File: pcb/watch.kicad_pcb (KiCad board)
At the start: 2 copper layers, 2 parts, among them U1 nRF52840, U3 MAX-M10S

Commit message: sus2
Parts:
- added AE1: Antenna, JLCImport:KH-GPS181804-WY, F.Cu at (152.5, 97.0)
- added BT2: Battery_Cell, Connector_JST:JST_PH_S2B-PH-SM4-TB_1x02-1MP_P2.00mm_Horizontal, F.Cu at (172.7, 113.3)
- added C10: 12pF, Capacitor_SMD:C_0402_1005Metric, F.Cu at (167.6, 99.3)
- added C11: 12pF, Capacitor_SMD:C_0402_1005Metric, F.Cu at (167.6, 101.3)
- added C12: 1uF, Capacitor_SMD:C_0402_1005Metric, F.Cu at (170.5, 89.5)
- added C13: 47nF, Capacitor_SMD:C_0603_1608Metric, F.Cu at (164.2, 97.3)
- added C14: 100pF, Capacitor_SMD:C_0402_1005Metric, F.Cu at (170.5, 91.4)
- added C15: 4.7uF, Capacitor_SMD:C_0603_1608Metric, F.Cu at (164.2, 99.8)
- added C17: 12pF, Capacitor_SMD:C_0402_1005Metric, F.Cu at (170.5, 93.4)
- added C18: 12pF, Capacitor_SMD:C_0402_1005Metric, F.Cu at (170.5, 95.4)
- added C19: 10uF, Capacitor_SMD:C_0603_1608Metric, F.Cu at (164.2, 102.3)
- added C2: 100nF, Capacitor_SMD:C_0402_1005Metric, F.Cu at (167.6, 89.5)
- added C20: 22uF, Capacitor_SMD:C_0805_2012Metric, F.Cu at (151.2, 126.2)
- added C21: 1uF, Capacitor_SMD:C_0402_1005Metric, F.Cu at (170.5, 97.3)
- added C22: 1uF, Capacitor_SMD:C_0402_1005Metric, F.Cu at (170.5, 99.3)
- added C23: 1uF, Capacitor_SMD:C_0402_1005Metric, F.Cu at (170.5, 101.3)
- added C24: 4.7uF, Capacitor_SMD:C_0603_1608Metric, F.Cu at (164.2, 104.8)
- added C25: 100nF, Capacitor_SMD:C_0402_1005Metric, F.Cu at (173.3, 89.5)
- added C26: 1uF, Capacitor_SMD:C_0402_1005Metric, F.Cu at (173.3, 91.4)
- added C27: 100nF, Capacitor_SMD:C_0402_1005Metric, F.Cu at (173.3, 93.4)
- added C28: 100nF, Capacitor_SMD:C_0402_1005Metric, F.Cu at (173.3, 95.4)
- added C3: 100nF, Capacitor_SMD:C_0402_1005Metric, F.Cu at (167.6, 91.4)
- added C4: 100nF, Capacitor_SMD:C_0402_1005Metric, F.Cu at (167.6, 93.4)
- added C5: 100nF, Capacitor_SMD:C_0402_1005Metric, F.Cu at (167.6, 95.4)
- added C6: 100nF, Capacitor_SMD:C_0402_1005Metric, F.Cu at (167.6, 97.3)
- added C7: 4.7uF, Capacitor_SMD:C_0603_1608Metric, F.Cu at (164.2, 89.7)
- added C8: 4.7uF, Capacitor_SMD:C_0603_1608Metric, F.Cu at (164.2, 92.2)
- added C9: 4.7uF, Capacitor_SMD:C_0603_1608Metric, F.Cu at (164.2, 94.8)
- added D2: red, LED_SMD:LED_0603_1608Metric, F.Cu at (169.6, 126.2)
- added D3: green, LED_SMD:LED_0805_2012Metric, F.Cu at (145.2, 124.2)
- added F2: 1A/1.8A, Fuse:Fuse_1206_3216Metric_Pad1.42x1.75mm_HandSolder, F.Cu at (146.0, 121.0)
- added J1: USB_C_Receptacle_USB2.0_14P, Connector_USB:USB_C_Receptacle_G-Switch_GT-USB-7010ASV, F.Cu at (161.7, 113.0)
- added R3: 100k, Resistor_SMD:R_0402_1005Metric, F.Cu at (169.0, 119.9)
- added R6: 1.5k, Resistor_SMD:R_0402_1005Metric, F.Cu at (169.0, 121.9)
- added R7: 1.5k, Resistor_SMD:R_0402_1005Metric, F.Cu at (169.0, 123.9)
- added R8: 1.5k, Resistor_SMD:R_0402_1005Metric, F.Cu at (171.9, 119.9)
- added R9: 1.5k, Resistor_SMD:R_0402_1005Metric, F.Cu at (171.9, 121.9)
- added SW1: 10k, Resistor_SMD:R_0402_1005Metric, F.Cu at (171.9, 123.9)
- added SW2: 10k, Resistor_SMD:R_0402_1005Metric, F.Cu at (174.8, 119.9)
- added SW3: 10k, Resistor_SMD:R_0402_1005Metric, F.Cu at (174.8, 121.9)
- added SW4: 10k, Resistor_SMD:R_0402_1005Metric, F.Cu at (174.8, 123.9)
- added U4: nRF52840, Package_DFN_QFN:Nordic_AQFN-73-1EP_7x7mm_P0.5mm, F.Cu at (160.9, 122.8)
- added U5: MAX-M10S, RF_GPS:ublox_MAX, F.Cu at (149.4, 113.5)
- added U7: BQ24074RGT, Package_DFN_QFN:VQFN-16-1EP_3x3mm_P0.5mm_EP1.6x1.6mm, F.Cu at (152.0, 122.0)
- added U8: TPS7A20xxxDQN, Package_SON:Texas_X2SON-4_1x1mm_P0.65mm, F.Cu at (173.2, 126.2)
- added Y1: RV-3028-C7, Package_SON:MicroCrystal_C7_SON-8_1.5x3.2mm_P0.9mm, F.Cu at (168.3, 104.9)
- added Y2: USBLC6-2SC6, Package_TO_SOT_SMD:SOT-23-6, F.Cu at (172.8, 104.7)
- U1: value nRF52840 -> 5.1k; footprint Package_DFN_QFN:Nordic_AQFN-73-1EP_7x7mm_P0.5mm -> Resistor_SMD:R_0603_1608Metric_Pad0.98x0.95mm_HandSolder
- U3: value MAX-M10S -> SW_Push
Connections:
- U3 pad 11: unconnected-(U3-RF_IN-Pad11) -> Net-(AE1-A)
- U3 pad 18: unconnected-(U3-~{SAFEBOOT}-Pad18) -> P0.15
- U3 pad 2: unconnected-(U3-TXD-Pad2) -> P0.13
- U3 pad 3: unconnected-(U3-RXD-Pad3) -> P0.14
- U3 pad 6: unconnected-(U3-V_BCKP-Pad6) -> +3V3
- U3 pad 7: +3V3 -> +3V0_GPS
- U3 pad 8: +3V3 -> +3V0_GPS
- U3 pad 9: unconnected-(U3-~{RESET}-Pad9) -> P0.16

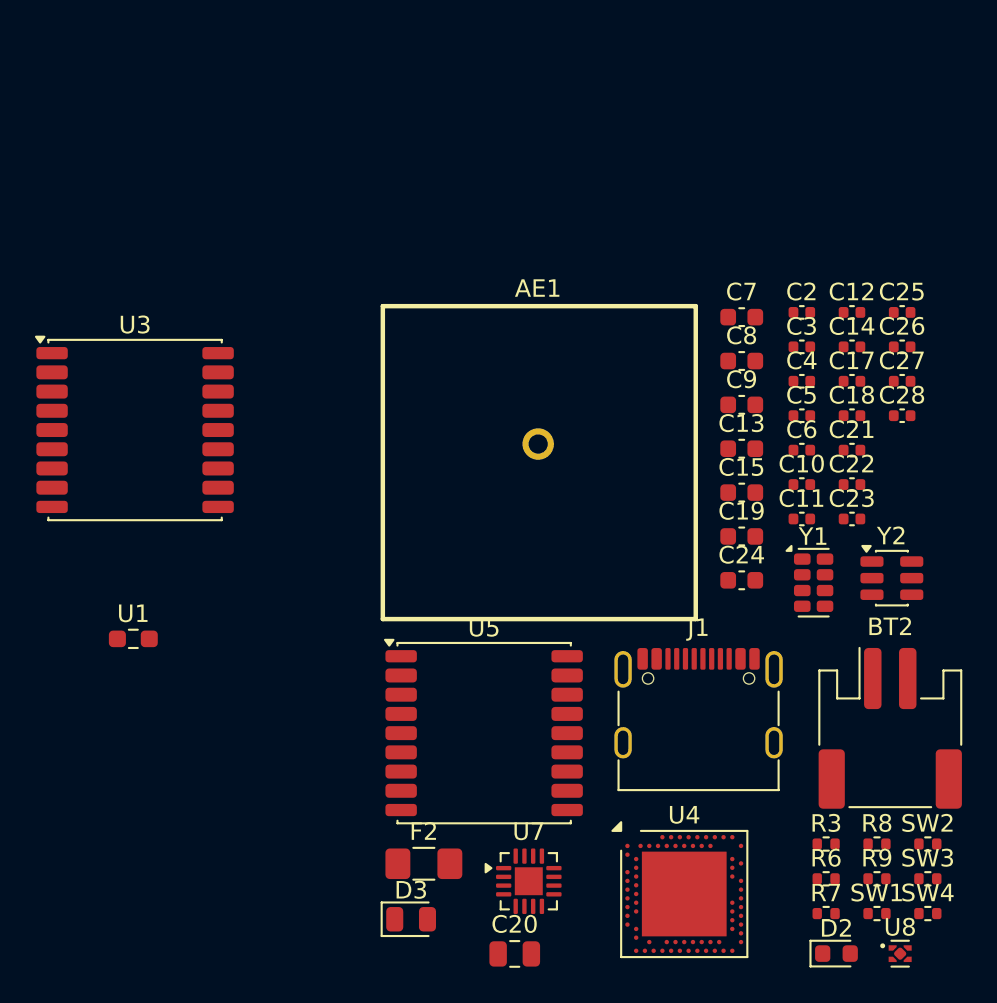
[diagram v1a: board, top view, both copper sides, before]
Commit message: fix symbols getting absolutely goofed up
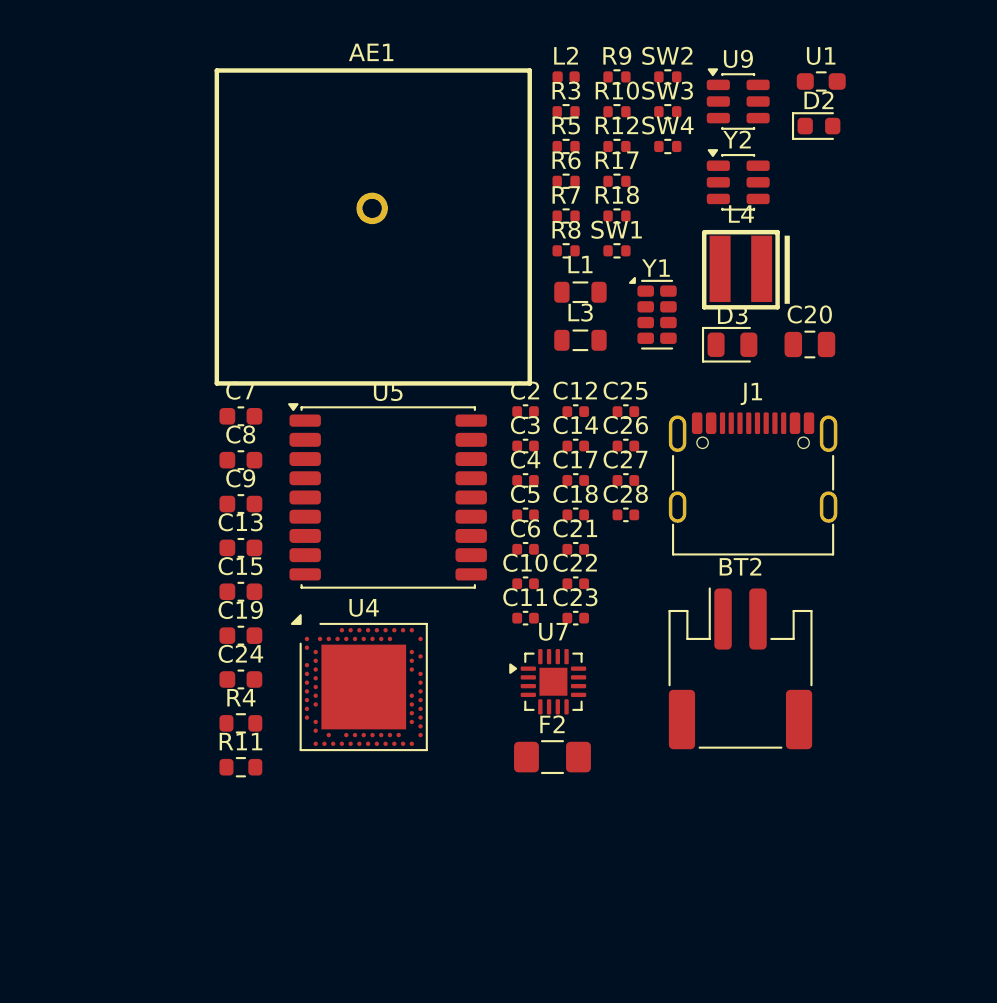
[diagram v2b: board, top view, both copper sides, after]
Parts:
- removed U3: SW_Push, RF_GPS:ublox_MAX
- removed U8: TPS7A20xxxDQN, Package_SON:Texas_X2SON-4_1x1mm_P0.65mm
- added L1: 10uH, Inductor_SMD:L_0805_2012Metric, F.Cu at (154.9, 88.3)
- added L2: 15nH, Inductor_SMD:L_0402_1005Metric, F.Cu at (154.1, 76.0)
- added L3: 10uH, Inductor_SMD:L_0805_2012Metric, F.Cu at (154.9, 91.1)
- added L4: 0.47uH, JLCImport:XFL4015-471MEC, F.Cu at (164.1, 87.0)
- added R10: 1.18k, Resistor_SMD:R_0402_1005Metric, F.Cu at (157.0, 78.0)
- added R11: 1.13k, Resistor_SMD:R_0603_1608Metric, F.Cu at (135.5, 115.5)
- added R12: 46.4k, Resistor_SMD:R_0402_1005Metric, F.Cu at (157.0, 80.0)
- added R17: 4.12k, Resistor_SMD:R_0402_1005Metric, F.Cu at (157.0, 82.0)
- added R18: 4.12k, Resistor_SMD:R_0402_1005Metric, F.Cu at (157.0, 84.0)
- added R4: 511k, Resistor_SMD:R_0603_1608Metric, F.Cu at (135.5, 113.0)
- added R5: 91k, Resistor_SMD:R_0402_1005Metric, F.Cu at (154.1, 80.0)
- added U9: USBLC6-2SC6, Package_TO_SOT_SMD:SOT-23-6, F.Cu at (164.0, 77.4)
- Y2: value USBLC6-2SC6 -> 32.768KHz
- moved U1 50.7 mm to (168.7, 76.3)
- moved R9 48.2 mm to (157.0, 76.0)
- moved D2 47.4 mm to (168.6, 78.8)
- moved SW4 46.3 mm to (159.9, 80.0)
- moved SW2 46.3 mm to (159.9, 76.0)
- moved SW3 46.3 mm to (159.9, 78.0)
- moved R3 44.5 mm to (154.1, 78.0)
- moved R7 42.6 mm to (154.1, 84.0)
- moved R6 42.6 mm to (154.1, 82.0)
- moved SW1 40.7 mm to (157.0, 85.9)
- moved C20 38.7 mm to (168.1, 91.3)
- moved R8 38.3 mm to (154.1, 85.9)
- moved D3 37.7 mm to (163.6, 91.3)
- moved C13 29.2 mm to (135.5, 102.9)
- moved C15 29.2 mm to (135.5, 105.5)
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
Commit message: sussy
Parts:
- removed AE1: Antenna, JLCImport:KH-GPS181804-WY
- removed BT2: Battery_Cell, Connector_JST:JST_PH_S2B-PH-SM4-TB_1x02-1MP_P2.00mm_Horizontal
- removed C23: 1uF, Capacitor_SMD:C_0402_1005Metric
- removed C24: 4.7uF, Capacitor_SMD:C_0603_1608Metric
- removed D3: green, LED_SMD:LED_0805_2012Metric
- removed F2: 1A/1.8A, Fuse:Fuse_1206_3216Metric_Pad1.42x1.75mm_HandSolder
- removed R17, R18: 4.12k, Resistor_SMD:R_0402_1005Metric
- removed U7: BQ24074RGT, Package_DFN_QFN:VQFN-16-1EP_3x3mm_P0.5mm_EP1.6x1.6mm
- removed U9: USBLC6-2SC6, Package_TO_SOT_SMD:SOT-23-6
- removed the Y1 at (159.3, 89.6)
- removed the Y2 at (164.0, 82.0)
- added BT1: Battery_Cell, Connector_JST:JST_PH_S2B-PH-SM4-TB_1x02-1MP_P2.00mm_Horizontal, F.Cu at (162.7, 95.6)
- added C1: 100nF, Capacitor_SMD:C_0402_1005Metric, F.Cu at (150.4, 81.0)
- added C16: 22pF, Capacitor_SMD:C_0402_1005Metric, F.Cu at (153.3, 82.9)
- added D1: green, LED_SMD:LED_0805_2012Metric, F.Cu at (151.3, 107.1)
- added F1: 1A/1.8A, Fuse:Fuse_1206_3216Metric_Pad1.42x1.75mm_HandSolder, F.Cu at (152.0, 103.9)
- added R1: 4.12k, Resistor_SMD:R_0402_1005Metric, F.Cu at (162.0, 85.0)
- added R2: 4.12k, Resistor_SMD:R_0402_1005Metric, F.Cu at (162.0, 87.0)
- added U2: USBLC6-2SC6, Package_TO_SOT_SMD:SOT-23-6, F.Cu at (160.2, 103.6)
- added U3: MAX-M10S, RF_GPS:ublox_MAX, F.Cu at (172.8, 83.9)
- added U6: BQ24074RGT, Package_DFN_QFN:VQFN-16-1EP_3x3mm_P0.5mm_EP1.6x1.6mm, F.Cu at (152.0, 94.4)
- added U8: RV-3028-C7, Package_SON:MicroCrystal_C7_SON-8_1.5x3.2mm_P0.9mm, F.Cu at (151.1, 99.8)
- added Y1: RV-3028-C7, Package_SON:MicroCrystal_C7_SON-8_1.5x3.2mm_P0.9mm, F.Cu at (155.1, 99.8)
- added Y1: 32MHz, Crystal:Crystal_SMD_2016-4Pin_2.0x1.6mm, F.Cu at (169.0, 75.3)
- added Y2: 32.768KHz, Package_TO_SOT_SMD:SOT-23-6, F.Cu at (160.2, 108.2)
- added Y2: 32.768KHz, JLCImport:Q13FC1350000400, F.Cu at (152.2, 110.9)
- C10, C11: value 12pF -> 4.7uF; footprint Capacitor_SMD:C_0402_1005Metric -> Capacitor_SMD:C_0603_1608Metric
- C12, C22: value 1uF -> 4.7uF; footprint Capacitor_SMD:C_0402_1005Metric -> Capacitor_SMD:C_0603_1608Metric
- C13: value 47nF -> 1uF; footprint Capacitor_SMD:C_0603_1608Metric -> Capacitor_SMD:C_0402_1005Metric
- C14: value 100pF -> 47nF; footprint Capacitor_SMD:C_0402_1005Metric -> Capacitor_SMD:C_0603_1608Metric
- C15: value 4.7uF -> 22pF; footprint Capacitor_SMD:C_0603_1608Metric -> Capacitor_SMD:C_0402_1005Metric
- C17: value 12pF -> 10uF; footprint Capacitor_SMD:C_0402_1005Metric -> Capacitor_SMD:C_0603_1608Metric
- C18: value 12pF -> 1uF
- C19: value 10uF -> 1uF; footprint Capacitor_SMD:C_0603_1608Metric -> Capacitor_SMD:C_0402_1005Metric
- C2: value 100nF -> 4.7uF; footprint Capacitor_SMD:C_0402_1005Metric -> Capacitor_SMD:C_0603_1608Metric
- C3, C4: value 100nF -> 12pF
- C5: value 100nF -> 100pF
- C7, C8, C9: value 4.7uF -> 100nF; footprint Capacitor_SMD:C_0603_1608Metric -> Capacitor_SMD:C_0402_1005Metric
- L2: value 15nH -> 10uH; footprint Inductor_SMD:L_0402_1005Metric -> Inductor_SMD:L_0805_2012Metric
- L3: value 10uH -> 15nH; footprint Inductor_SMD:L_0805_2012Metric -> Inductor_SMD:L_0402_1005Metric
- R10: value 1.18k -> 46.4k
- R11: value 1.13k -> 1.5k; footprint Resistor_SMD:R_0603_1608Metric -> Resistor_SMD:R_0402_1005Metric
- R12: value 46.4k -> 1.5k
- R3: value 100k -> 511k; footprint Resistor_SMD:R_0402_1005Metric -> Resistor_SMD:R_0603_1608Metric
- R4: value 511k -> 91k; footprint Resistor_SMD:R_0603_1608Metric -> Resistor_SMD:R_0402_1005Metric
- R5: value 91k -> 100k
- R6: value 1.5k -> 1.18k
- R9: value 1.5k -> 1.13k; footprint Resistor_SMD:R_0402_1005Metric -> Resistor_SMD:R_0603_1608Metric
- U1: value 5.1k -> nRF52840; footprint Resistor_SMD:R_0603_1608Metric_Pad0.98x0.95mm_HandSolder -> Package_DFN_QFN:Nordic_AQFN-73-1EP_7x7mm_P0.5mm
- U4: value nRF52840 -> TPS63802DLAR; footprint Package_DFN_QFN:Nordic_AQFN-73-1EP_7x7mm_P0.5mm -> JLCImport:TPS63802DLAR
- U5: value MAX-M10S -> TPS7A20xxxDQN; footprint RF_GPS:ublox_MAX -> Package_SON:Texas_X2SON-4_1x1mm_P0.65mm
- moved U4 59.2 mm to (198.0, 90.2)
- moved R11 38.6 mm to (159.1, 85.0)
- moved R4 38.2 mm to (159.1, 83.0)
- moved L4 35.3 mm to (170.2, 121.7)
- moved D2 33.3 mm to (155.5, 109.5)
- moved C13 29.9 mm to (153.3, 79.0)
- moved U1 29.1 mm to (172.9, 105.0)
- moved L2 28.7 mm to (165.0, 102.6)
- moved C15 27.2 mm to (153.3, 84.9)
- moved C10 26.2 mm to (147.0, 79.3)
- moved C19 26.1 mm to (153.3, 88.8)
- moved C11 25.7 mm to (147.0, 81.8)
- moved R9 25.4 mm to (147.0, 99.3)
- moved C7 22.2 mm to (150.4, 79.0)
- moved C9 20.2 mm to (150.4, 86.9)
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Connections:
- C10 pad 1: GND -> /mcu/VDD_nRF
- C10 pad 2: Net-(U1-XC1) -> GND
- C11 pad 1: GND -> +BATT
- C11 pad 2: Net-(U1-XC2) -> GND
- C12 pad 1: /mcu/DEC4 -> VBUS
- C14 pad 1: Net-(U1-DEC3) -> /mcu/DEC4
- C15 pad 1: VBUS -> GND
- C15 pad 2: GND -> Net-(U1-XL1/P0.00)
- C17 pad 1: GND -> +BATT
- C17 pad 2: Net-(U1-XL2/P0.01) -> GND
- C18 pad 1: GND -> +3V3_ALT
- C18 pad 2: Net-(U1-XL1/P0.00) -> GND
- C19 pad 1: +BATT -> +3V0_GPS
- C19 pad 2: GND -> Net-(C19-Pad2)
- C2 pad 1: Net-(U1-DEC1) -> Net-(U1-DECUSB)
- C21 pad 1: +3V3_ALT -> VBUS
- C22 pad 1: +3V0_GPS -> VBAT_RAW
- C3 pad 1: /mcu/VDD_nRF -> GND
- C3 pad 2: GND -> Net-(U1-XC1)
- C4 pad 1: /mcu/VDD_nRF -> GND
- C4 pad 2: GND -> Net-(U1-XC2)
- C5 pad 1: /mcu/VDD_nRF -> Net-(U1-DEC3)
- C7 pad 1: /mcu/VDD_nRF -> Net-(U1-DEC1)
- C8 pad 1: +BATT -> /mcu/VDD_nRF
- C9 pad 1: Net-(U1-DECUSB) -> /mcu/VDD_nRF
- J1 pad SH: (no net) -> GND
- L1 pad 1: Net-(L1-Pad1) -> /mcu/VDD_nRF
- L1 pad 2: Net-(U1-DCC) -> Net-(U1-DCCH)
- L2 pad 1: /mcu/DEC4 -> Net-(L2-Pad1)
- L2 pad 2: Net-(L1-Pad1) -> Net-(U1-DCC)
- L3 pad 1: /mcu/VDD_nRF -> /mcu/DEC4
- L3 pad 2: Net-(U1-DCCH) -> Net-(L2-Pad1)
- R10 pad 1: GND -> Net-(U6-TS)
- R10 pad 2: Net-(U5-TMR) -> GND
- R11 pad 1: GND -> Net-(D1-A)
- R11 pad 2: Net-(U5-ITERM) -> +BATT
- R12 pad 1: Net-(U5-TS) -> Net-(D2-A)
- R12 pad 2: GND -> +BATT
- R3 pad 1: +BATT -> +3V3_ALT
- R3 pad 2: Net-(U4-PG) -> Net-(U4-FB)
- R4 pad 1: +3V3_ALT -> Net-(U4-FB)
- R4 pad 2: Net-(U4-FB) -> GND
- R5 pad 1: Net-(U4-FB) -> +BATT
- R5 pad 2: GND -> Net-(U4-PG)
- R6 pad 1: Net-(D3-A) -> GND
- R6 pad 2: +BATT -> Net-(U6-TMR)
- R7 pad 1: Net-(D2-A) -> GND
- R7 pad 2: +BATT -> Net-(U6-ILIM)
- R8 pad 2: Net-(U5-ILIM) -> Net-(U6-ISET)
- R9 pad 2: Net-(U5-ISET) -> Net-(U6-ITERM)
- U5 pad 1: Net-(U5-TS) -> +3V0_GPS
- U5 pad 2: VBAT_RAW -> GND
- U5 pad 3: VBAT_RAW -> P0.26
- U5 pad 4: P1.04 -> +3V3_ALT
- U5 pad 5: P1.06 -> Net-(C19-Pad2)

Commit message: done for the day
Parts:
- removed C15, C16: 22pF, Capacitor_SMD:C_0402_1005Metric
- removed SW1, SW2, SW3, SW4: 10k, Resistor_SMD:R_0402_1005Metric
- removed the Y1 at (155.1, 99.8)
- removed the Y1 at (169.0, 75.3)
- removed Y2: 32.768KHz, Package_TO_SOT_SMD:SOT-23-6
- removed Y2: 32.768KHz, JLCImport:Q13FC1350000400
- added AE1: Antenna, JLCImport:KH-GPS181804-WY, F.Cu at (133.9, 81.4)
- added DS1: ~, JLCImport:5034801000, F.Cu at (162.3, 114.7)
- added SW6: PWR, JLCImport:SK-3296S-01-L1, F.Cu at (163.0, 108.5)
- added Y1: 32MHz, Crystal:Crystal_SMD_2016-4Pin_2.0x1.6mm, F.Cu at (180.5, 78.3)
- moved U3 43.2 mm to (133.5, 102.0)
- moved D1 38.9 mm to (180.8, 81.7)
- moved R6 35.5 mm to (173.7, 114.5)
- moved R5 34.7 mm to (173.7, 112.5)
- moved U6 33.8 mm to (181.1, 111.7)
- moved C7 32.7 mm to (176.6, 98.6)
- moved C13 31.5 mm to (179.4, 96.6)
- moved C28 31.5 mm to (182.3, 102.6)
- moved C25 31.5 mm to (182.3, 96.6)
- moved C26 31.5 mm to (182.3, 98.6)
- moved C27 31.5 mm to (182.3, 100.6)
- moved F1 31.5 mm to (181.0, 116.1)
- moved R4 31.2 mm to (173.7, 110.5)
- moved R8 31.2 mm to (176.6, 106.5)
- moved R12 31.0 mm to (176.6, 112.5)
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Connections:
- BT1 pad 1: VBAT_RAW -> Net-(BT1-+)
- U1 pad D2: Net-(U1-XL1/P0.00) -> LF_EXT_CLK
- U1 pad F2: Net-(U1-XL2/P0.01) -> GND
- U8 pad 1: unconnected-(U8-CLKOUT-Pad1) -> LF_EXT_CLK

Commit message: amogus
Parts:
- added R15: 10k, Resistor_SMD:R_0402_1005Metric, F.Cu at (162.0, 73.0)
- added R16: 10k, Resistor_SMD:R_0402_1005Metric, F.Cu at (162.0, 75.0)
- added R17: 10k, Resistor_SMD:R_0402_1005Metric, F.Cu at (162.0, 77.0)
- added U9: TPS2116DRL, Package_TO_SOT_SMD:SOT-583-8, F.Cu at (165.3, 74.0)
- moved AE1 11.8 mm to (136.4, 92.9)
- moved U3 9.95 mm to (136.8, 111.4)
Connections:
- C21 pad 1: VBUS -> V_CHARGE
- U1 pad A14: unconnected-(U1-P1.15-PadA14) -> P1.15
- U6 pad 13: VBUS -> V_CHARGE

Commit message: change to 4layer
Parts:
- added J2: Adafruit Wireless Chg Module, Connector_PinHeader_2.54mm:PinHeader_1x02_P2.54mm_Vertical, F.Cu at (145.8, 75.3)
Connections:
- U9 pad 1: unconnected-(U9-GND-Pad1) -> GND
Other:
- copper layers 2 -> 4

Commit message: starting le leyout
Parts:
- removed SW6: PWR, JLCImport:SK-3296S-01-L1
- added C15: 100nF, Capacitor_SMD:C_0402_1005Metric, F.Cu at (89.3, 103.3)
- BT1: value Battery_Cell -> LiPo
- moved C18 88.8 mm to (90.9, 104.8), turned to 180 degrees
- moved C28 88.6 mm to (93.8, 100.9), turned to -90 degrees
- moved C19 87.2 mm to (92.3, 103.3), turned to -90 degrees
- moved U8 83.2 mm to (94.6, 97.8), turned to 180 degrees
- moved U5 81.5 mm to (90.8, 103.3), turned to -90 degrees
- moved C9 78.4 mm to (98.6, 95.0), turned to 180 degrees
- moved C7 78.0 mm to (98.6, 96.0), turned to 180 degrees
- moved C13 77.4 mm to (102.1, 93.0), turned to 90 degrees
- moved R12 77.3 mm to (109.4, 74.2), turned to 90 degrees
- moved R11 76.1 mm to (110.7, 72.5), turned to 180 degrees
- moved U6 75.2 mm to (114.0, 77.8), turned to 180 degrees
- moved L3 73.6 mm to (101.1, 93.0), turned to 90 degrees
- moved C11 73.5 mm to (96.8, 103.0), turned to -90 degrees
- moved D2 73.4 mm to (110.2, 76.2), turned to 180 degrees
- moved Y1 72.1 mm to (110.1, 93.8), turned to 90 degrees
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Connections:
- C22 pad 1: VBAT_RAW -> Net-(BT1-+)
- J1 pad A6: /mcu/D+ -> Net-(J1-D+-PadA6)
- J1 pad A7: /mcu/D- -> Net-(J1-D--PadA7)
- J1 pad B6: /mcu/D+ -> Net-(J1-D+-PadA6)
- J1 pad B7: /mcu/D- -> Net-(J1-D--PadA7)
- U2 pad 1: /mcu/D- -> Net-(J1-D--PadA7)
- U2 pad 3: /mcu/D+ -> Net-(J1-D+-PadA6)
- U2 pad 4: unconnected-(U2-I/O2-Pad4) -> /mcu/D+
- U2 pad 6: unconnected-(U2-I/O1-Pad6) -> /mcu/D-
- U6 pad 2: VBAT_RAW -> Net-(BT1-+)
- U6 pad 3: VBAT_RAW -> Net-(BT1-+)
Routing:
- net /mcu/VDD_nRF: track 0.00 -> 12.0 mm
- net Net-(F1-Pad1): track 0.00 -> 11.0 mm
- net GND: track 0.00 -> 6.51 mm
- net Net-(U1-XC1): track 0.00 -> 5.50 mm
- net /mcu/DEC4: track 0.00 -> 5.32 mm
- net Net-(U1-XC2): track 0.00 -> 5.11 mm
- net Net-(J1-D--PadA7): track 0.00 -> 4.75 mm
- net Net-(J1-D+-PadA6): track 0.00 -> 4.75 mm
- net Net-(U1-DCCH): track 0.00 -> 3.52 mm
- net Net-(U1-DCC): track 0.00 -> 3.48 mm
- net Net-(J1-CC1): track 0.00 -> 3.45 mm
- net Net-(U1-DEC3): track 0.00 -> 2.36 mm
- net Net-(D1-K): track 0.00 -> 2.07 mm
- net Net-(D2-K): track 0.00 -> 1.97 mm
- net Net-(U1-DEC1): track 0.00 -> 1.94 mm
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- added copper zone on B.Cu, net GND
- added copper zone on F.Cu, net GND
- added copper zone on In1.Cu, net GND
- added copper zone on In4.Cu, net GND
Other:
- board outline added: 47.2 x 35.5 mm
- copper layers 4 -> 6

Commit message: mogus
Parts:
- removed AE1: Antenna, JLCImport:KH-GPS181804-WY
- added E1: DSGP.1575.18.4.A.02, antrenna:XCVR_DSGP.1575.18.4.A.02, F.Cu at (91.0, 80.5)
- moved BT1 0.54 mm to (123.1, 76.6)
- moved R7 0.16 mm to (110.8, 78.7)
- moved C15 0.10 mm to (89.4, 103.3)
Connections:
- C25 pad 1: P1.14 -> P1.07
- DS1 pad 10: P1.10 -> P1.01
- DS1 pad 6: P1.14 -> P1.07
- DS1 pad 7: P1.13 -> P1.06
- DS1 pad 8: P1.12 -> P1.04
- DS1 pad 9: P1.11 -> P1.02
- R15 pad 2: P0.23 -> P0.04
- R16 pad 2: P0.27 -> P0.26
- R17 pad 2: P1.15 -> P1.13
- U1 pad A12: unconnected-(U1-AIN0/P0.02-PadA12) -> P0.02
- U1 pad AD12: TIMEPULSE -> unconnected-(U1-P0.17-PadAD12)
- U1 pad AD8: P0.13 -> TIMEPULSE
- U1 pad J1: unconnected-(U1-AIN2/P0.04-PadJ1) -> P0.04
- U1 pad L1: unconnected-(U1-P0.06-PadL1) -> P0.06
- U1 pad M2: unconnected-(U1-TRACECLK/P0.07-PadM2) -> P0.07
- U1 pad N1: unconnected-(U1-P0.08-PadN1) -> P0.08
- U1 pad T2: unconnected-(U1-TRACEDATA2/P0.11-PadT2) -> P0.11
- U1 pad U1: unconnected-(U1-TRACEDATA1/P0.12-PadU1) -> P0.12
- U3 pad 18: P0.15 -> P0.06
- U3 pad 2: P0.13 -> P0.08
- U3 pad 3: P0.14 -> P0.12
- U3 pad 9: P0.16 -> P0.11
- U5 pad 3: P0.26 -> unconnected-(U5-EN-Pad3)
- U6 pad 4: P1.04 -> P1.11
- U6 pad 5: P1.06 -> P1.10
- U6 pad 6: P1.05 -> P1.15
- U8 pad 3: P0.23 -> P0.04
- U8 pad 4: P0.27 -> P0.26
- U9 pad 8: P1.15 -> P1.13
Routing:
- net +BATT: track 1.55 -> 70.8 mm, vias 0 -> 5
- net +3V3: track 0.00 -> 50.0 mm, vias 0 -> 4
- net VBUS: track 0.00 -> 48.7 mm, vias 0 -> 3
- net +3V3_ALT: track 0.00 -> 40.8 mm, vias 0 -> 2
- net /mcu/VDD_nRF: track 12.0 -> 39.1 mm, vias 0 -> 3
- net P1.15: track 0.00 -> 25.4 mm, vias 0 -> 2
- net P1.10: track 0.00 -> 24.5 mm, vias 0 -> 2
- net P1.11: track 0.00 -> 24.5 mm, vias 0 -> 2
- net P0.06: track 0.00 -> 21.8 mm, vias 0 -> 2
- net P0.25: track 0.00 -> 21.5 mm
- net P0.08: track 0.00 -> 18.0 mm, vias 0 -> 2
- net TIMEPULSE: track 0.00 -> 17.6 mm, vias 0 -> 2
- net P1.01: track 0.00 -> 16.7 mm, vias 0 -> 2
- net /mcu/D-: track 0.00 -> 16.5 mm, vias 0 -> 2
- net P1.02: track 0.00 -> 16.5 mm
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- added copper zone on F.Cu, net +3V3
- added copper zone on F.Cu, net Net-(BT1-+)
- added copper zone on F.Cu, net Net-(J2-Pin_2)
- added copper zone on F.Cu, net Net-(U4-L1)
- added copper zone on F.Cu, net Net-(U4-L2)
